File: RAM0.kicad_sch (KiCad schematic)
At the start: 0 parts

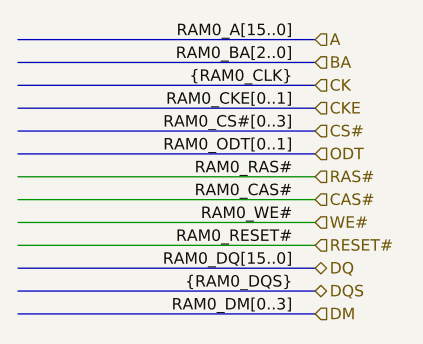
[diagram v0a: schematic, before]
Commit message: design CPU DDR
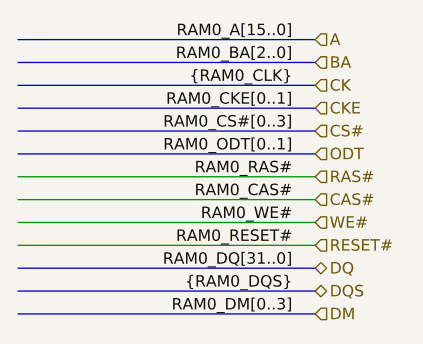
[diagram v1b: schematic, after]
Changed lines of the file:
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@@
 		(rev "1.0.0")
 	)
-	(bus_alias "RAM1_CK"
-		(members "RAM1_CK0+" "RAM1_CK0-" "RAM1_CK1+" "RAM1_CK1-")
+	(bus_alias "RAM1_CLK"
+		(members "RAM1_CLK0+" "RAM1_CLK0-" "RAM1_CLK1+" "RAM1_CLK1-")
 	)
 	(bus
@@
 		)
 	)
-	(label "RAM0_DQ[15..0]"
+	(label "RAM0_DQ[31..0]"
 		(at 172.72 109.22 180)
 		(effects

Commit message: design CPU-RK3399 eMMC Controller
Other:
- company: (none) -> TickLab
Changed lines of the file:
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@@
 	(paper "A4")
 	(title_block
-		(date "2026-01-09")
+		(date "2026-01-14")
 		(rev "1.0.0")
+		(company "TickLab")
 	)
 	(bus_alias "RAM1_CLK"

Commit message: design DDR
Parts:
- added U18, U19: MT41K256M16TW-107:P, footprints:BGA96C80P9X16_800X1400X110, symbol component_library:ICs/MT41K256M16TW-107P
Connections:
- net CAS#: now also U18.K3 (~{CAS}), U19.K3 (~{CAS})
- net RAS#: now also U18.J3 (~{RAS}), U19.J3 (~{RAS})
- net RESET#: now also U18.T2 (~{RESET}), U19.T2 (~{RESET})
- net WE#: now also U18.L3 (~{WE}), U19.L3 (~{WE})
- new net +1V35_VCC_DDR: U18.A1 (VDDQ), U18.A8 (VDDQ), U18.B2 (VDD), U18.C1 (VDDQ), U18.C9 (VDDQ), U18.D2 (VDDQ), U18.D9 (VDD), U18.E9 (VDDQ), U18.F1 (VDDQ), U18.G7 (VDD), U18.H2 (VDDQ), U18.H9 (VDDQ), U18.K2 (VDD), U18.K8 (VDD), U18.N1 (VDD), U18.N9 (VDD), U18.R1 (VDD), U18.R9 (VDD), U19.A1 (VDDQ), U19.A8 (VDDQ), U19.B2 (VDD), U19.C1 (VDDQ), U19.C9 (VDDQ), U19.D2 (VDDQ), U19.D9 (VDD), U19.E9 (VDDQ), U19.F1 (VDDQ), U19.G7 (VDD), U19.H2 (VDDQ), U19.H9 (VDDQ), U19.K2 (VDD), U19.K8 (VDD), U19.N1 (VDD), U19.N9 (VDD), U19.R1 (VDD), U19.R9 (VDD)
- new net GND: U18.A9 (VSS), U18.B1 (VSSQ), U18.B3 (VSS), U18.B9 (VSSQ), U18.D1 (VSSQ), U18.D8 (VSSQ), U18.E1 (VSS), U18.E2 (VSSQ), U18.E8 (VSSQ), U18.F9 (VSSQ), U18.G1 (VSSQ), U18.G8 (VSS), U18.G9 (VSSQ), U18.J2 (VSS), U18.J8 (VSS), U18.M1 (VSS), U18.M9 (VSS), U18.P1 (VSS), U18.P9 (VSS), U18.T1 (VSS), U18.T9 (VSS), U19.A9 (VSS), U19.B1 (VSSQ), U19.B3 (VSS), U19.B9 (VSSQ), U19.D1 (VSSQ), U19.D8 (VSSQ), U19.E1 (VSS), U19.E2 (VSSQ), U19.E8 (VSSQ), U19.F9 (VSSQ), U19.G1 (VSSQ), U19.G8 (VSS), U19.G9 (VSSQ), U19.J2 (VSS), U19.J8 (VSS), U19.M1 (VSS), U19.M9 (VSS), U19.P1 (VSS), U19.P9 (VSS), U19.T1 (VSS), U19.T9 (VSS)
- new net RAM0_A0: U18.N3 (A0), U19.N3 (A0)
- new net RAM0_A1: U18.P7 (A1), U19.P7 (A1)
- new net RAM0_A10: U18.L7 (A10/AP), U19.L7 (A10/AP)
- new net RAM0_A11: U18.R7 (A11), U19.R7 (A11)
- new net RAM0_A12: U18.N7 (A12/~{BC}), U19.N7 (A12/~{BC})
- new net RAM0_A13: U18.T3 (A13), U19.T3 (A13)
- new net RAM0_A14: U18.T7 (A14), U19.T7 (A14)
- new net RAM0_A15: U18.M7 (NC), U19.M7 (NC)
- new net RAM0_A2: U18.P3 (A2), U19.P3 (A2)
- new net RAM0_A3: U18.N2 (A3), U19.N2 (A3)
- new net RAM0_A4: U18.P8 (A4), U19.P8 (A4)
- new net RAM0_A5: U18.P2 (A5), U19.P2 (A5)
- new net RAM0_A6: U18.R8 (A6), U19.R8 (A6)
- new net RAM0_A7: U18.R2 (A7), U19.R2 (A7)
- new net RAM0_A8: U18.T8 (A8), U19.T8 (A8)
- new net RAM0_A9: U18.R3 (A9), U19.R3 (A9)
- new net RAM0_BA0: U18.M2 (BA0), U19.M2 (BA0)
- new net RAM0_BA1: U18.N8 (BA1), U19.N8 (BA1)
- new net RAM0_BA2: U18.M3 (BA2), U19.M3 (BA2)
- new net RAM0_CKE0: U18.K9 (CKE), U19.K9 (CKE)
- new net RAM0_CKE1: U18.J9 (NC), U19.J9 (NC)
- new net RAM0_CLK0+: U18.J7 (CK), U19.J7 (CK)
- new net RAM0_CLK0-: U18.K7 (~{CK}), U19.K7 (~{CK})
- new net RAM0_CS#0: U18.L2 (~{CS}), U19.L2 (~{CS})
- new net RAM0_CS#1: U18.L1 (NC), U19.L1 (NC)
- new net RAM0_DM0: U18.E7 (LDM)
- new net RAM0_DM1: U19.E7 (LDM)
- new net RAM0_DM2: U18.D3 (UDM)
- new net RAM0_DM3: U19.D3 (UDM)
- new net RAM0_DQ0: U18.E3 (DQ0)
- new net RAM0_DQ1: U18.F7 (DQ1)
- new net RAM0_DQ10: U18.C8 (DQ10)
- new net RAM0_DQ11: U18.C2 (DQ11)
- new net RAM0_DQ12: U18.A7 (DQ12)
- new net RAM0_DQ13: U18.A2 (DQ13)
- new net RAM0_DQ14: U18.B8 (DQ14)
- new net RAM0_DQ15: U18.A3 (DQ15)
- new net RAM0_DQ16: U19.E3 (DQ0)
- new net RAM0_DQ17: U19.F7 (DQ1)
- new net RAM0_DQ18: U19.F2 (DQ2)
- new net RAM0_DQ19: U19.F8 (DQ3)
- new net RAM0_DQ2: U18.F2 (DQ2)
- new net RAM0_DQ20: U19.H3 (DQ4)
- new net RAM0_DQ21: U19.H8 (DQ5)
- new net RAM0_DQ22: U19.G2 (DQ6)
- new net RAM0_DQ23: U19.H7 (DQ7)
- new net RAM0_DQ24: U19.D7 (DQ8)
- new net RAM0_DQ25: U19.C3 (DQ9)
- new net RAM0_DQ26: U19.C8 (DQ10)
- new net RAM0_DQ27: U19.C2 (DQ11)
- new net RAM0_DQ28: U19.A7 (DQ12)
- new net RAM0_DQ29: U19.A2 (DQ13)
- new net RAM0_DQ3: U18.F8 (DQ3)
- new net RAM0_DQ30: U19.B8 (DQ14)
- new net RAM0_DQ31: U19.A3 (DQ15)
- new net RAM0_DQ4: U18.H3 (DQ4)
- new net RAM0_DQ5: U18.H8 (DQ5)
- new net RAM0_DQ6: U18.G2 (DQ6)
- new net RAM0_DQ7: U18.H7 (DQ7)
- new net RAM0_DQ8: U18.D7 (DQ8)
- new net RAM0_DQ9: U18.C3 (DQ9)
- new net RAM0_DQS0+: U18.F3 (LDQS)
- new net RAM0_DQS0-: U18.G3 (~{LDQS})
- new net RAM0_DQS1+: U19.F3 (LDQS)
- new net RAM0_DQS1-: U19.G3 (~{LDQS})
- new net RAM0_DQS2+: U18.C7 (UDQS)
- new net RAM0_DQS2-: U18.B7 (~{UDQS})
- new net RAM0_DQS3+: U19.C7 (UDQS)
- new net RAM0_DQS3-: U19.B7 (~{UDQS})
- new net RAM0_ODT0: U18.K1 (ODT), U19.K1 (ODT)
- new net RAM0_ODT1: U18.J1 (NC), U19.J1 (NC)
